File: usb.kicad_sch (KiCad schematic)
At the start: 133 parts, among them J3 USB4105-GF-A, J4 WE_632723300011_alt_symbol, Q1 NX138BKMYL, Q2 NX138BKMYL, Q3 NX138BKMYL, U10 TUSB1046-DCI, U11 TPD4E05U06QDQARQ1, U12 AP22615, U13 TPD4E05U06QDQARQ1, U14 TPD4E05U06QDQARQ1, U15 TPD4E05U06QDQARQ1, U16 TPD4E05U06QDQARQ1, U5 FT230XQ-R, U6 TPS65988, U7 W25Q80DVUXIE_TR, U8 TPS7B8133DRVR, U9 AP22615

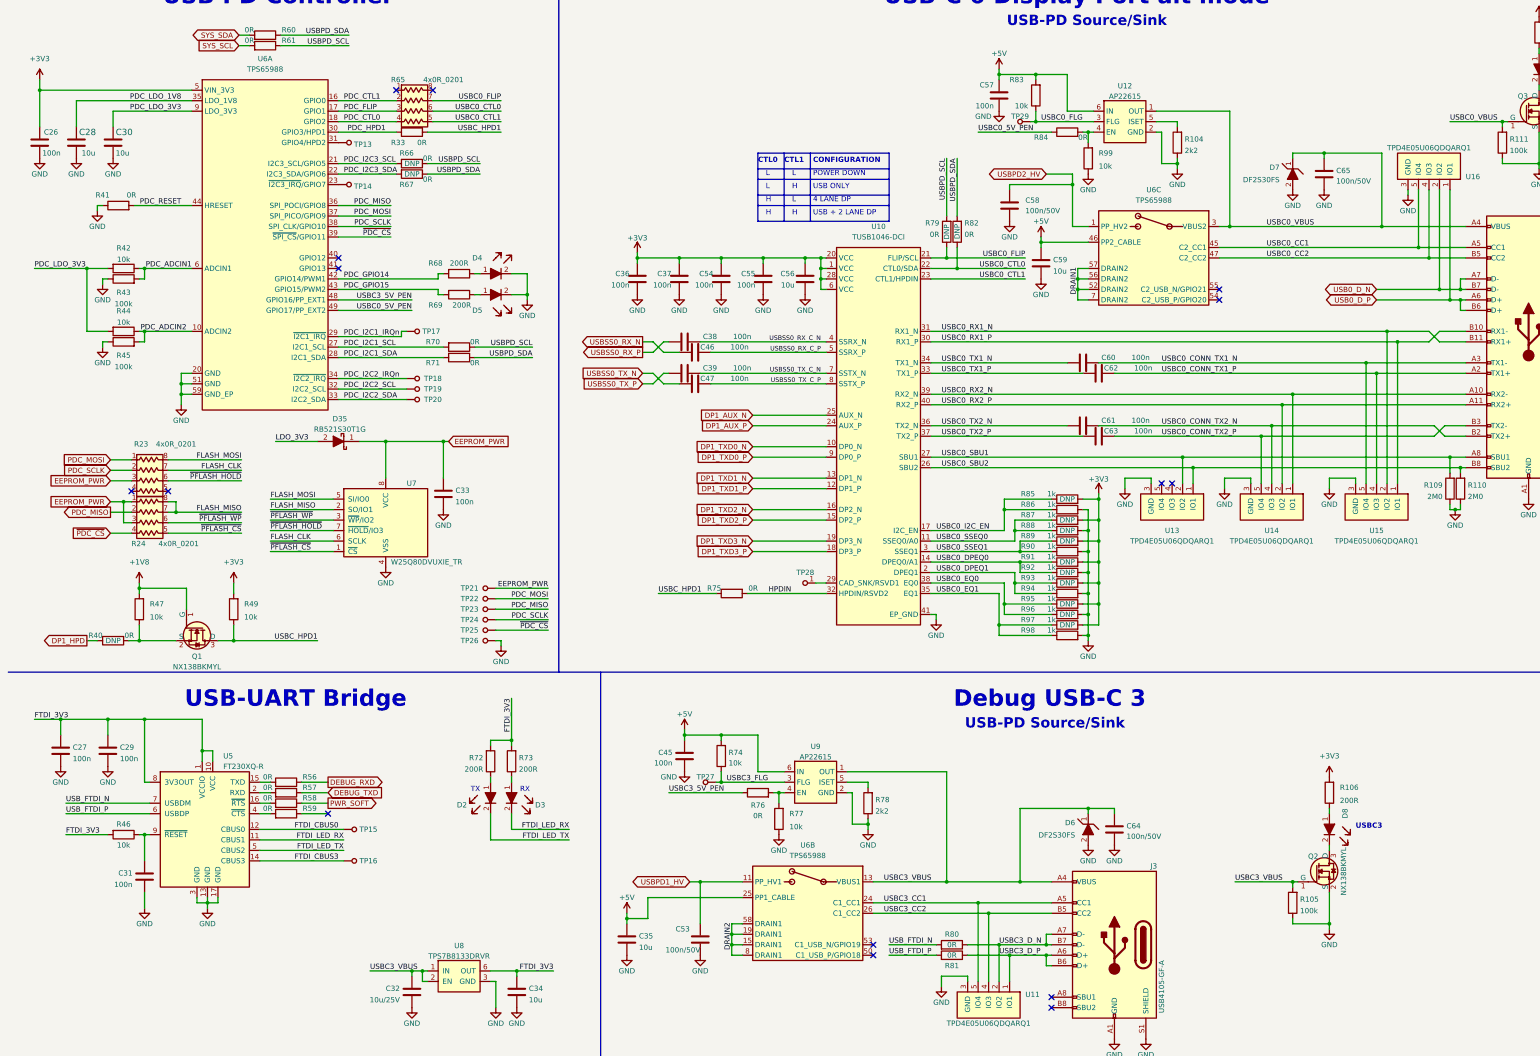
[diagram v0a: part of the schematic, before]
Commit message: Routed USB PD controller
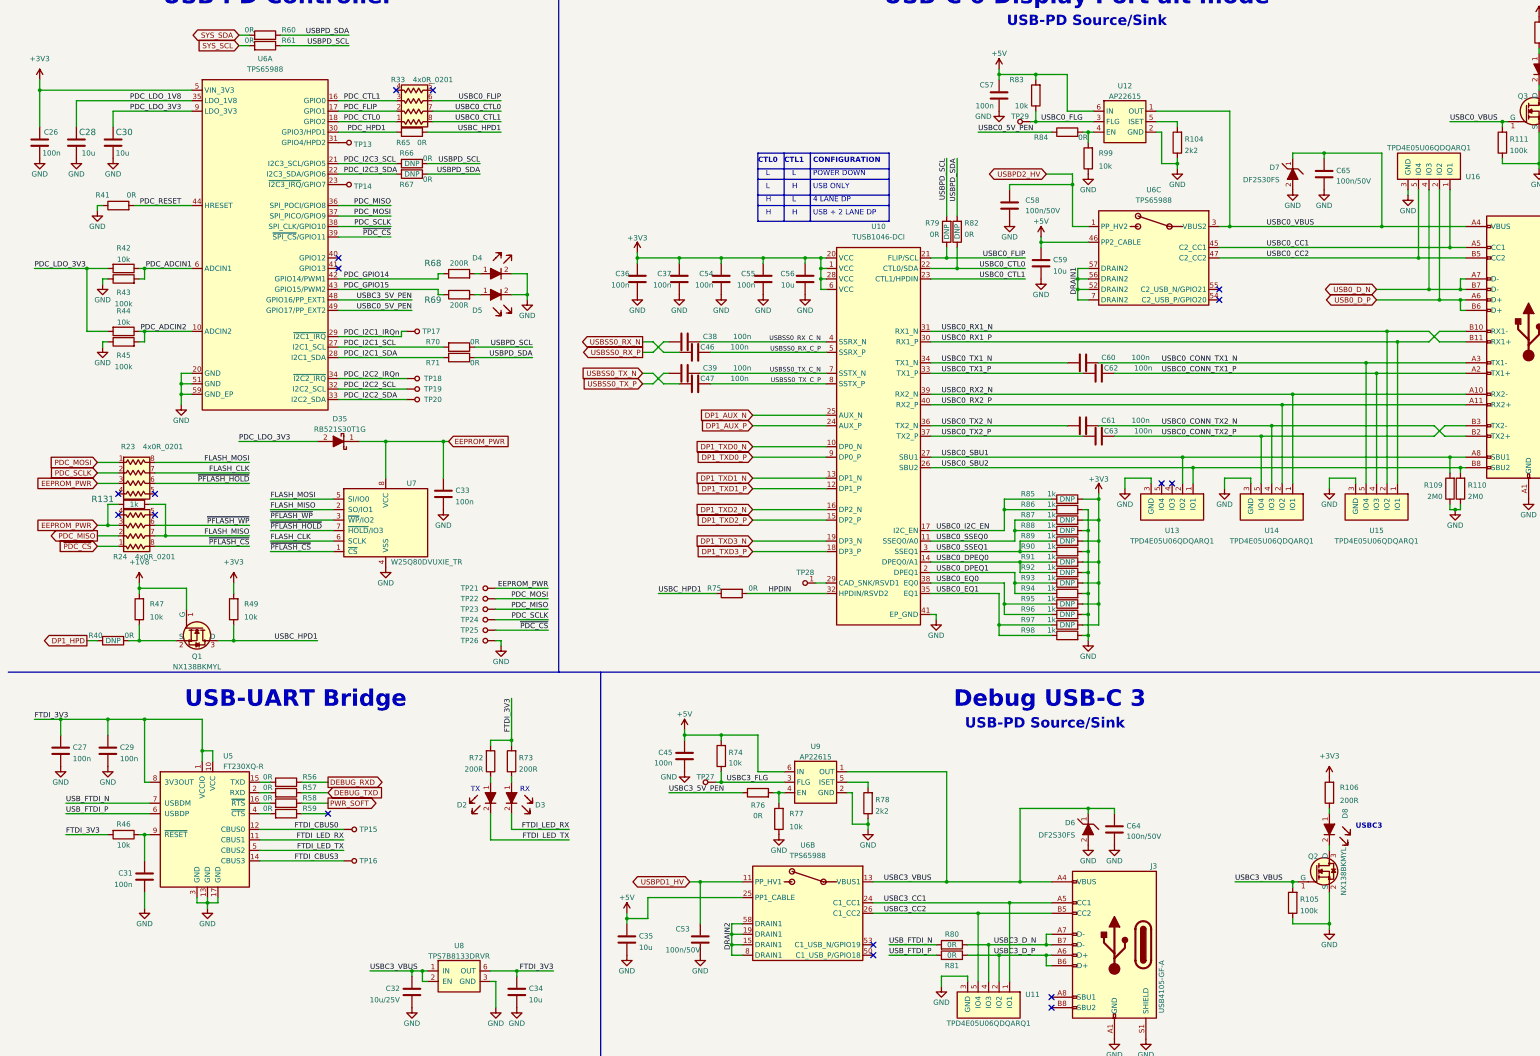
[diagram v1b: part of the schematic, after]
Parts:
- removed R68, R69: R_200R_0603, antmicro-footprints:0603-res, symbol antmicroResistors0603:R_200R_0603
- added R131: R_1k_0402, antmicro-footprints:0402-res, symbol antmicroResistors0402:R_1k_0402
- added R68, R69: R_200R_0402, antmicro-footprints:0402-res, symbol antmicroResistors0402:R_200R_0402
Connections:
- net LDO_3V3 is gone; now on net PDC_LDO_3V3: D35.2
- net EEPROM_PWR: now also R131.1; no longer R24.1
- net FLASH_MISO: now also R131.2; no longer R24.8
- net PDC_CTL0: now also R33.1; no longer R33.4
- net PDC_CTL1: now also R33.3; no longer R33.2
- net PDC_FLIP: now also R33.2; no longer R33.3
- net PDC_GPIO14: now also R68.1
- net PDC_GPIO15: now also R69.1
- net USB0_D_N: now also U16.4 (IO3), U16.7 (IO3); no longer U16.2 (IO2), U16.9 (IO2)
- net USB0_D_P: now also U16.2 (IO2), U16.9 (IO2); no longer U16.1 (IO1), U16.10 (IO1)
- net USBC0_CC1: now also U16.1 (IO1), U16.10 (IO1); no longer U16.5 (IO4), U16.6 (IO4)
- net USBC0_CC2: now also U16.5 (IO4), U16.6 (IO4); no longer U16.4 (IO3), U16.7 (IO3)
- net USBC0_CTL0: now also R33.7; no longer R33.6
- net USBC0_CTL1: now also R33.8; no longer R33.5
- net USBC0_FLIP: now also R33.6; no longer R33.7
- net USBC3_CC1: now also U11.1 (IO1), U11.10 (IO1); no longer U11.5 (IO4), U11.6 (IO4)
- net USBC3_CC2: now also U11.5 (IO4), U11.6 (IO4); no longer U11.4 (IO3), U11.7 (IO3)
- net USBC3_D_N: now also U11.4 (IO3), U11.7 (IO3); no longer J3.A6 (D+), J3.B6 (D+), R81.1, U11.1 (IO1), U11.10 (IO1), U11.2 (IO2), U11.9 (IO2)
- net ~{PDC_CS}: now also R24.1; no longer R24.4
- net ~{PFLASH_CS}: now also R24.8; no longer R24.5
- net at D5.1: now also R69.2
- net at D4.1: now also R68.2
- new net USBC3_D_P: J3.A6 (D+), J3.B6 (D+), R81.1, U11.2 (IO2), U11.9 (IO2)
- no-connect marks 15 -> 17
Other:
- moved on the sheet: R23, R24

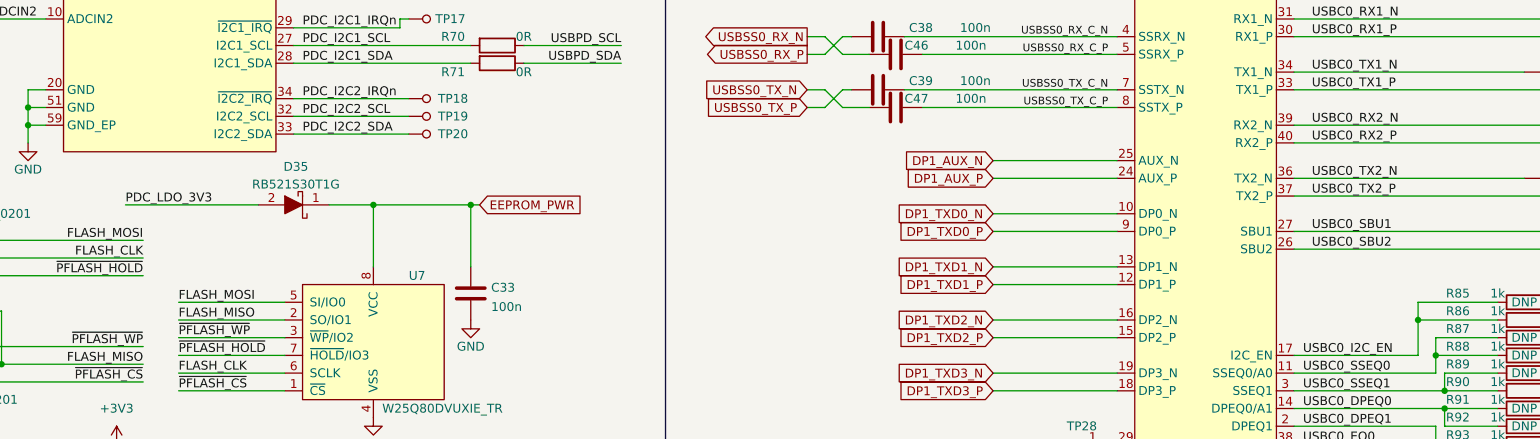
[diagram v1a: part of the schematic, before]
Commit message: Started routing USB-C DP switch
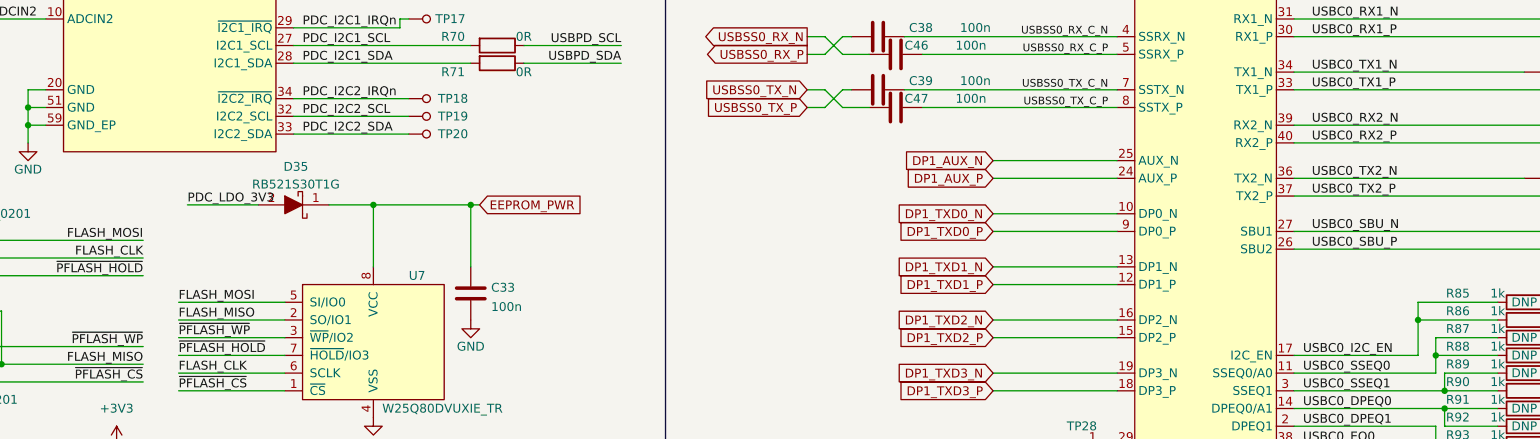
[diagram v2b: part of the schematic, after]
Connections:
- net USBC0_SBU1 renamed USBC0_SBU_N
- net USBC0_SBU2 renamed USBC0_SBU_P
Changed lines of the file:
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@@
     (stroke (width 0) (type default) (color 0 0 0 0))
   )
-  (wire (pts (xy 68.58 125.73) (xy 87.63 125.73))
+  (wire (pts (xy 77.47 125.73) (xy 87.63 125.73))
     (stroke (width 0) (type default) (color 0 0 0 0))
   )
@@
     (effects (font (size 1.27 1.27)) (justify left bottom))
   )
-  (label "USBC0_SBU2" (at 238.76 132.08 0)
+  (label "USBC0_SBU_P" (at 238.76 132.08 0)
     (effects (font (size 1.27 1.27)) (justify left bottom))
   )
@@
     (effects (font (size 1.27 1.27)) (justify left bottom))
   )
-  (label "PDC_LDO_3V3" (at 68.58 125.73 0)
+  (label "PDC_LDO_3V3" (at 77.47 125.73 0)
     (effects (font (size 1.27 1.27)) (justify left bottom))
   )
@@
     (effects (font (size 1.27 1.27)) (justify left bottom))
   )
-  (label "USBC0_SBU1" (at 238.76 129.54 0)
+  (label "USBC0_SBU_N" (at 238.76 129.54 0)
     (effects (font (size 1.27 1.27)) (justify left bottom))
   )

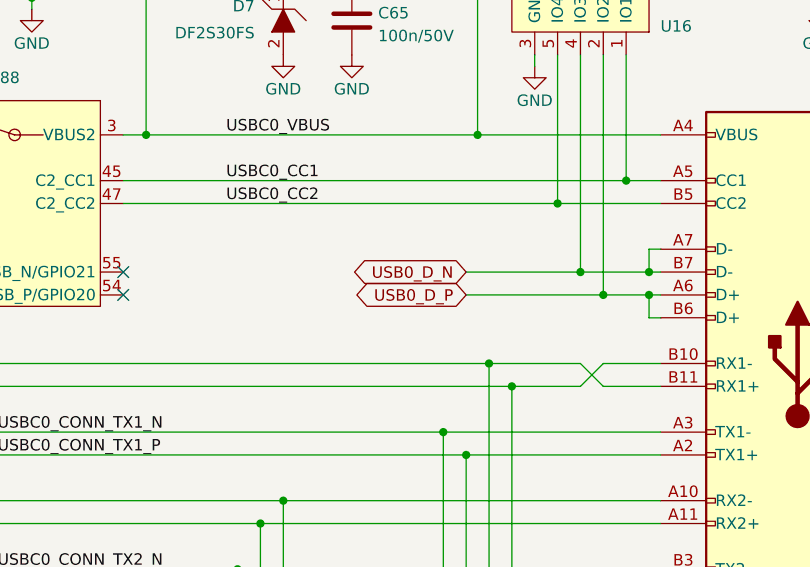
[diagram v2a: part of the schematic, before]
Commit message: Routed USB connector
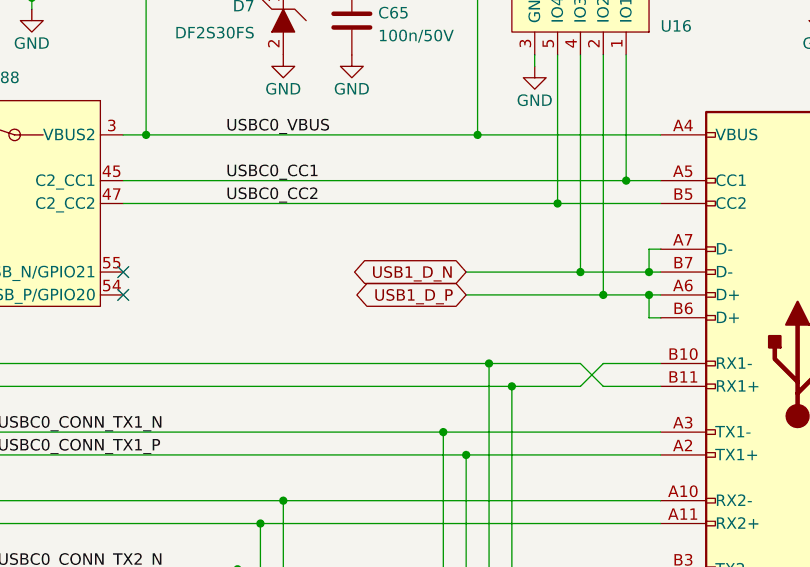
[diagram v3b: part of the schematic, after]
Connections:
- net USB0_D_N renamed USB1_D_N
- net USB0_D_P renamed USB1_D_P
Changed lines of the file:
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@@
-    )
-  )
-  (global_label "USB0_D_P" (shape bidirectional) (at 344.17 91.44 180)
-    (effects (font (size 1.27 1.27)) (justify right))
-    (property "Intersheet References" "${INTERSHEET_REFS}" (id 0) (at 330.835 91.44 0)
-      (effects (font (size 1.1 1.1)) (justify right))
     )
   )
@@
     (property "Intersheet References" "${INTERSHEET_REFS}" (id 0) (at 104.14 210.82 0)
       (effects (font (size 1.27 1.27)) (justify left))
+    )
+  )
+  (global_label "USB1_D_P" (shape bidirectional) (at 344.17 91.44 180)
+    (effects (font (size 1.27 1.27)) (justify right))
+    (property "Intersheet References" "${INTERSHEET_REFS}" (id 0) (at 330.2 91.44 0)
+      (effects (font (size 1.1 1.1)) (justify right))
     )
   )
@@
     )
   )
-  (global_label "USB0_D_N" (shape bidirectional) (at 344.17 88.9 180)
+  (global_label "USB1_D_N" (shape bidirectional) (at 344.17 88.9 180)
     (effects (font (size 1.27 1.27)) (justify right))
-    (property "Intersheet References" "${INTERSHEET_REFS}" (id 0) (at 330.835 88.9 0)
+    (property "Intersheet References" "${INTERSHEET_REFS}" (id 0) (at 330.1476 88.9 0)
       (effects (font (size 1.1 1.1)) (justify right))
     )

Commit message: Routed USB 2.0; Routed 5V and 3V3 power rails
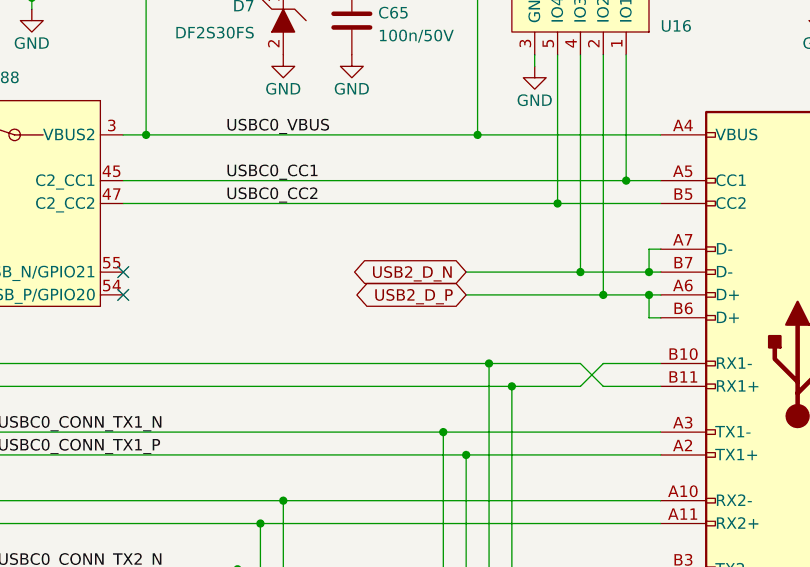
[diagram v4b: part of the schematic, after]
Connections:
- net USB1_D_N renamed USB2_D_N
- net USB1_D_P renamed USB2_D_P
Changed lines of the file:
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@@
-    )
-  )
-  (global_label "USB1_D_P" (shape bidirectional) (at 344.17 91.44 180)
-    (effects (font (size 1.27 1.27)) (justify right))
-    (property "Intersheet References" "${INTERSHEET_REFS}" (id 0) (at 330.2 91.44 0)
-      (effects (font (size 1.1 1.1)) (justify right))
     )
   )
@@
     )
   )
-  (global_label "USB1_D_N" (shape bidirectional) (at 344.17 88.9 180)
-    (effects (font (size 1.27 1.27)) (justify right))
-    (property "Intersheet References" "${INTERSHEET_REFS}" (id 0) (at 330.1476 88.9 0)
-      (effects (font (size 1.1 1.1)) (justify right))
-    )
-  )
   (global_label "PDC_MOSI" (shape input) (at 34.29 130.81 180)
     (effects (font (size 1.27 1.27)) (justify right))
@@
     )
   )
+  (global_label "USB2_D_N" (shape bidirectional) (at 344.17 88.9 180)
+    (effects (font (size 1.27 1.27)) (justify right))
+    (property "Intersheet References" "${INTERSHEET_REFS}" (id 0) (at 330.835 88.9 0)
+      (effects (font (size 1.1 1.1)) (justify right))
+    )
+  )
   (global_label "DP1_HPD" (shape output) (at 31.75 173.99 180)
     (effects (font (size 1.27 1.27)) (justify right))
@@
     )
   )
+  (global_label "USB2_D_P" (shape bidirectional) (at 344.17 91.44 180)
+    (effects (font (size 1.27 1.27)) (justify right))
+    (property "Intersheet References" "${INTERSHEET_REFS}" (id 0) (at 330.835 91.44 0)
+      (effects (font (size 1.1 1.1)) (justify right))
+    )
+  )
